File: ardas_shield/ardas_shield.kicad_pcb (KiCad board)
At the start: 2 copper layers, 68.8 x 53.4 mm, 39 parts, among them CON1 SD_Card, IC1 DS1307, P1 CONN_10, P10 CONN_01X03, P2 CONN_8, P3 CONN_8, P4 CONN_ICSP, P5 CONN_6, P6 TTL_COMM, P7 CONN_01X03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

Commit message: rename Ardas
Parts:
- V4, V5, V6: footprint 1pin -> kicad-gfa local:MountingHole_3mm
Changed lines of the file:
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@@
     (links 152)
     (no_connects 0)
-    (area 26.206268 60.1726 264.729686 136.733281)
+    (area 46.862999 67.932299 116.078001 121.716801)
     (thickness 1.6002)
     (drawings 68)
@@
     )
   )
-  (module 1pin locked (layer Front)
-    (at 113.005 113.876)
-    (descr "module 1 pin (ou trou mecanique de percage)")
-    (tags DEV)
-    (path 1pin)
-    (fp_text reference V5 (at 0 -3.048) (layer F.SilkS) hide
-      (effects (font (size 1.016 1.016) (thickness 0.254)))
-    )
-    (fp_text value "" (at 0 2.794) (layer F.SilkS) hide
-      (effects (font (size 1.016 1.016) (thickness 0.254)))
-    )
-    (fp_circle (center 0.00254 0.00254) (end 1.39192 1.04648) (layer F.SilkS) (width 0.381))
-    (pad 1 thru_hole circle (at 0 0) (size 2.54 2.54) (drill 2.54) (layers *.Cu *.Mask F.SilkS))
-  )
   (module Pin_Headers:Pin_Header_Straight_1x08 locked (layer Back)
     (at 74.93 119.037 270)
@@
       (rotate (xyz 0 0 90))
     )
-  )
-  (module 1pin locked (layer Front)
-    (at 113.081 85.885)
-    (descr "module 1 pin (ou trou mecanique de percage)")
-    (tags DEV)
-    (path 1pin)
-    (fp_text reference V4 (at -2.29108 1.61036) (layer F.SilkS) hide
-      (effects (font (size 1.016 1.016) (thickness 0.254)))
-    )
-    (fp_text value "" (at 0 2.794) (layer F.SilkS) hide
-      (effects (font (size 1.016 1.016) (thickness 0.254)))
-    )
-    (fp_circle (center 0.00254 0.00254) (end 1.53924 0.81026) (layer F.SilkS) (width 0.381))
-    (pad 1 thru_hole circle (at 0 0) (size 2.54 2.54) (drill 2.54) (layers *.Cu *.Mask F.SilkS))
-  )
-  (module 1pin locked (layer Front)
-    (at 62.2808 70.8736)
-    (descr "module 1 pin (ou trou mecanique de percage)")
-    (tags DEV)
-    (path 1pin)
-    (fp_text reference V6 (at 4.6736 -8.6614) (layer F.SilkS) hide
-      (effects (font (size 1.016 1.016) (thickness 0.254)))
-    )
-    (fp_text value "" (at 0 2.794) (layer F.SilkS) hide
-      (effects (font (size 1.016 1.016) (thickness 0.254)))
-    )
-    (fp_circle (center 0 0.00508) (end 1.45288 0.93472) (layer F.SilkS) (width 0.381))
-    (pad 1 thru_hole circle (at 0 0) (size 2.54 2.54) (drill 2.54) (layers *.Cu *.Mask F.SilkS))
   )
   (module Capacitors_SMD:C_0805 (layer Front)
@@
     (tags "resistor array")
     (attr smd)
-    (fp_text reference RP1 (at 0 -3.5 180) (layer F.SilkS)
+    (fp_text reference RP1 (at 0 -3.556 180) (layer F.SilkS)
       (effects (font (size 1 1) (thickness 0.15)))
     )
@@
   (module RTC_Ardas_test:small_no_jumper (layer Front)
     (at 48.768 74.1553 270)
-    (fp_text reference JP1 (at 0 2.54 270) (layer F.SilkS)
+    (fp_text reference JP1 (at 0 -2.54 270) (layer F.SilkS)
       (effects (font (size 1 1) (thickness 0.15)))
     )
@@
       (net 1 GND) (solder_mask_margin 0.5))
   )
+  (module "kicad-gfa local:MountingHole_3mm" locked (layer Front)
+    (at 62.2808 70.8736)
+    (descr "Mounting hole, Befestigungsbohrung, 3mm, No Annular, Kein Restring,")
+    (tags "Mounting hole, Befestigungsbohrung, 3mm, No Annular, Kein Restring,")
+    (path 1pin)
+    (fp_text reference V6 (at 0 -4.0005) (layer F.SilkS) hide
+      (effects (font (size 1 1) (thickness 0.15)))
+    )
+    (fp_text value "" (at 1.00076 5.00126) (layer F.Fab) hide
+      (effects (font (size 1 1) (thickness 0.15)))
+    )
+    (fp_circle (center 0 0) (end 3 0) (layer Cmts.User) (width 0.381))
+    (pad 1 thru_hole circle (at 0 0) (size 3 3) (drill 3) (layers))
+  )
+  (module "kicad-gfa local:MountingHole_3mm" locked (layer Front)
+    (at 113.081 85.885)
+    (descr "Mounting hole, Befestigungsbohrung, 3mm, No Annular, Kein Restring,")
+    (tags "Mounting hole, Befestigungsbohrung, 3mm, No Annular, Kein Restring,")
+    (path 1pin)
+    (fp_text reference V4 (at 0 -4.0005) (layer F.SilkS) hide
+      (effects (font (size 1 1) (thickness 0.15)))
+    )
+    (fp_text value "" (at 1.00076 5.00126) (layer F.Fab) hide
+      (effects (font (size 1 1) (thickness 0.15)))
+    )
+    (fp_circle (center 0 0) (end 3 0) (layer Cmts.User) (width 0.381))
+    (pad 1 thru_hole circle (at 0 0) (size 3 3) (drill 3) (layers))
+  )
+  (module "kicad-gfa local:MountingHole_3mm" locked (layer Front)
+    (at 113.005 113.876)
+    (descr "Mounting hole, Befestigungsbohrung, 3mm, No Annular, Kein Restring,")
+    (tags "Mounting hole, Befestigungsbohrung, 3mm, No Annular, Kein Restring,")
+    (path 1pin)
+    (fp_text reference V5 (at 0 -4.0005) (layer F.SilkS) hide
+      (effects (font (size 1 1) (thickness 0.15)))
+    )
+    (fp_text value "" (at 1.00076 5.00126) (layer F.Fab) hide
+      (effects (font (size 1 1) (thickness 0.15)))
+    )
+    (fp_circle (center 0 0) (end 3 0) (layer Cmts.User) (width 0.381))
+    (pad 1 thru_hole circle (at 0 0) (size 3 3) (drill 3) (layers))
+  )
   (gr_text "ArDAS shield\n01-2016" (at 101.727 75.1078) (layer F.SilkS)

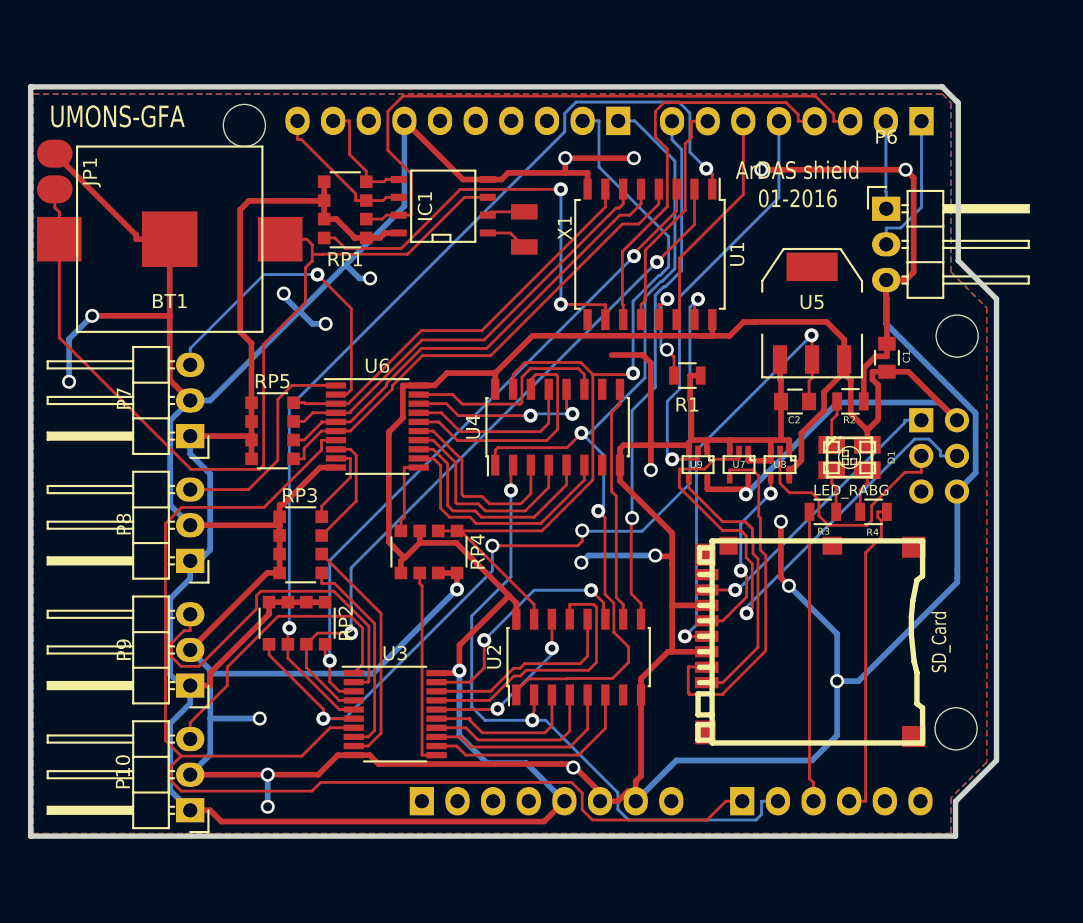
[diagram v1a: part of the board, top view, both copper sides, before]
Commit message: Updated ardas_shield geometry and microSD. Rerouted shield
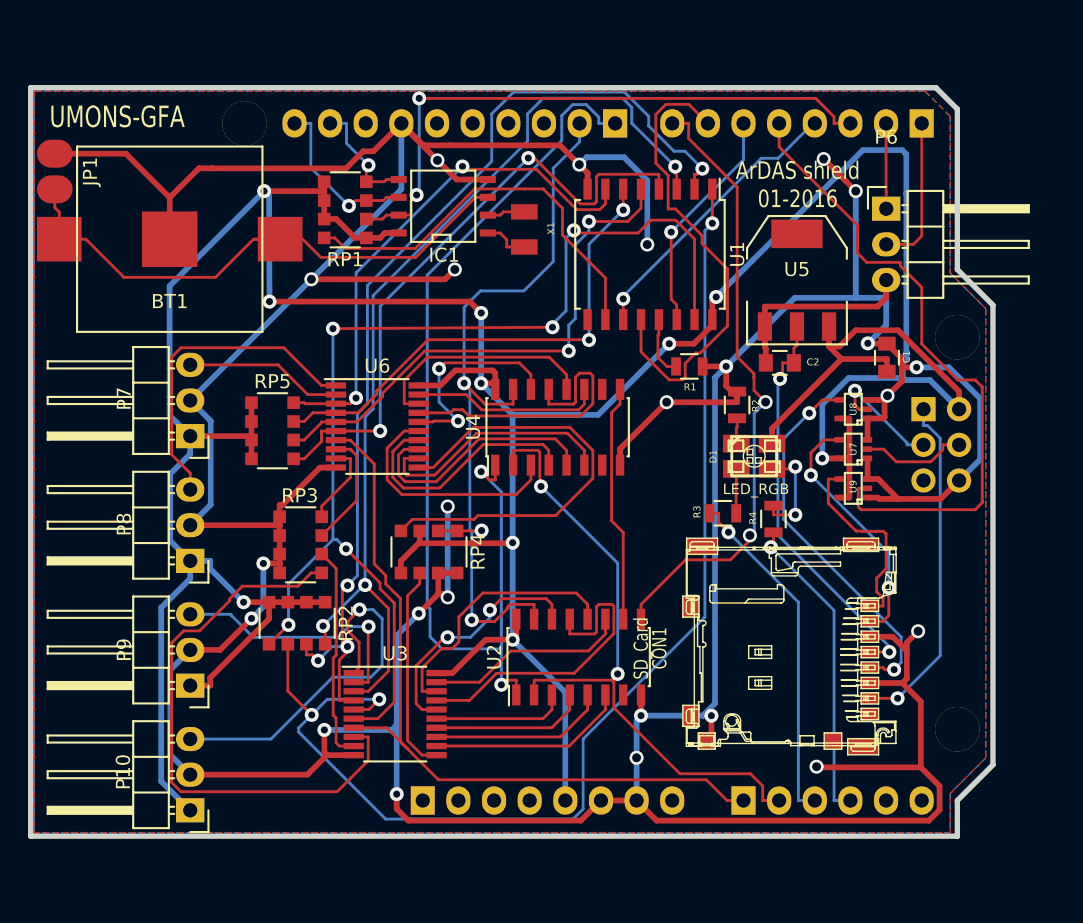
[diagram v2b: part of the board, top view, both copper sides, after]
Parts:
- CON1: footprint MyFootprints:microsd_socket -> kicad-gfa local:microSD_socket
- D1: value LED_RABG -> LED_RGB
- V4, V5, V6: footprint kicad-gfa local:MountingHole_3mm -> kicad-gfa local:MountingHole_125mil
- moved U9 11.2 mm to (105.7, 96.7), turned to 90 degrees
- moved U7 8.22 mm to (105.7, 93.9), turned to 90 degrees
- moved R2 8.08 mm to (97.4, 90.8), turned to 90 degrees
- moved R4 7.15 mm to (100.0, 98.9), turned to 270 degrees
- moved R3 7.13 mm to (96.4, 98.5)
- moved D1 6.80 mm to (98.6, 94.4)
- moved U8 6.55 mm to (105.7, 91.1), turned to 90 degrees
- moved C2 2.96 mm to (100.4, 87.8)
- moved U5 2.59 mm to (101.7, 81.9)
- moved CON1 1.51 mm to (101.3, 108.5), turned to 270 degrees
- moved P4 0.80 mm to (110.7, 91.1)
- moved R1 0.66 mm to (94.0, 88.0)
- moved P1 0.28 mm to (88.7, 70.7)
- moved P3 0.15 mm to (110.6, 70.7)
- moved V6 0.15 mm to (62.3, 70.7)
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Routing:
- net D14: track 90.9 -> 54.6 mm
- net +5V: track 249.4 -> 284.2 mm, vias 2 -> 10
- net MOSI: track 41.2 -> 7.62 mm, vias 1 -> 0
- net Net-(RP4-Pad4): track 5.64 -> 31.5 mm
- net Net-(RP3-Pad1): track 15.0 -> 40.7 mm
- net Net-(BT1-Pad1): track 63.1 -> 40.7 mm
- net Net-(RP2-Pad5): track 58.6 -> 79.9 mm, vias 4 -> 5
- net GND: track 377.5 -> 398.3 mm, vias 20 -> 24
- net Net-(RP2-Pad7): track 51.3 -> 72.0 mm, vias 2 -> 4
- net Net-(RP2-Pad8): track 48.6 -> 69.2 mm, vias 2 -> 3
- net Net-(RP2-Pad6): track 68.9 -> 85.9 mm, vias 2 -> 3
- net D06: track 16.8 -> 33.5 mm
- net D04: track 30.0 -> 46.3 mm, vias 1 -> 0
- net /SCK3: track 13.0 -> 27.0 mm
- net CH4: track 22.9 -> 11.3 mm, vias 1 -> 0
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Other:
- board size 68.8 x 53.4 mm -> 68.6 x 53.3 mm

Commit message: updated to v0.49
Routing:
- net Net-(D1-Pad3): track 7.38 -> 2.66 mm, vias 2 -> 0
- net GND: track 398.3 -> 396.4 mm, vias 24 -> 23
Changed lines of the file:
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@@
 (kicad_pcb (version 4) (host pcbnew 4.0.1-3.201512221402+6198~38~ubuntu14.04.1-stable)
   (general
-    (links 153)
+    (links 152)
     (no_connects 0)
-    (area 46.862999 67.995799 115.824001 121.716801)
+    (area 46.862999 60.1726 264.729686 132.9182)
     (thickness 1.6002)
     (drawings 63)
-    (tracks 1034)
+    (tracks 1028)
     (zones 0)
     (modules 39)
@@
     (title ArDAS_shield)
     (date 2016-01-13)
-    (rev 0.48)
+    (rev 0.49)
     (company UMONS-GFA)
     (comment 1 O.KAUFMANN)
@@
     (mod_text_width 0.3048)
     (pad_size 1.16 1.2)
-    (pad_drill 0.6)
+    (pad_drill 0)
     (pad_to_mask_clearance 0.254)
     (aux_axis_origin 125.349 130.2258)
@@
     (pad 1 smd rect (at -3.38328 -5.52196 270) (size 0.8 1.25) (layers Front F.Paste F.Mask)
       (net 5 /SEN3) (solder_mask_margin 0.1016) (clearance 0.254))
-    (pad GND smd rect (at 6.21792 6.11124 270) (size 1.16 1.2) (layers Front F.Paste F.Mask)
-      (net 1 GND) (solder_mask_margin 0.1016) (clearance 0.254))
+    (pad CD1 smd rect (at 6.21792 6.11124 270) (size 1.16 1.2) (layers Front F.Paste F.Mask)
+      (solder_mask_margin 0.1016) (clearance 0.254))
     (pad 9 smd rect (at 4.43992 7.25424 270) (size 1.5 1.15) (layers Front F.Paste F.Mask)
       (solder_mask_margin 0.1016) (clearance 0.254))
@@
     (effects (font (size 0.762 0.635) (thickness 0.16002)) (justify mirror))
   )
+  (segment (start 65.659 84.2518) (end 65.659 83.2358) (width 0.4064) (layer Back) (net 1))
+  (segment (start 65.659 83.2358) (end 65.8495 83.0453) (width 0.4064) (layer Back) (net 1))
+  (segment (start 67.056 81.8388) (end 65.8495 83.0453) (width 0.4064) (layer Back) (net 1))
+  (segment (start 58.42 90.4748) (end 63.9445 84.9503) (width 0.4064) (layer Back) (net 1))
+  (segment (start 63.9445 84.9503) (end 64.9605 84.9503) (width 0.4064) (layer Back) (net 1))
+  (segment (start 64.9605 84.9503) (end 65.659 84.2518) (width 0.4064) (layer Back) (net 1))
   (via (at 108.117049 90.133834) (size 1) (drill 0.635) (layers Front Back) (net 1))
   (segment (start 108.1405 90.1573) (end 108.1405 90.157285) (width 0.4064) (layer Back) (net 1))
@@
   (via (at 90.2335 115.9383) (size 1) (drill 0.635) (layers Front Back) (net 1))
   (segment (start 67.056 81.8388) (end 76.581 81.8388) (width 0.4064) (layer Front) (net 1))
-  (via (at 77.2795 81.1403) (size 1) (drill 0.635) (layers Front Back) (net 1))
   (segment (start 76.581 81.8388) (end 77.2795 81.1403) (width 0.4064) (layer Front) (net 1))
+  (via (at 77.2795 81.1403) (size 1) (drill 0.635) (layers Front Back) (net 1))
   (via (at 76.0409 73.3619) (size 1) (drill 0.635) (layers Front Back) (net 1))
   (segment (start 76.0409 73.3619) (end 76.0095 73.3933) (width 0.4064) (layer Back) (net 1))
@@
   (segment (start 106.693 96.0755) (end 107.4547 96.0755) (width 0.4064) (layer Front) (net 1))
   (segment (start 107.4547 96.0755) (end 108.8745 97.4953) (width 0.4064) (layer Front) (net 1))
-  (segment (start 95.5675 112.9411) (end 95.5675 114.39418) (width 0.4064) (layer Front) (net 1))
-  (segment (start 95.5675 114.39418) (end 95.23476 114.72692) (width 0.4064) (layer Front) (net 1))
   (via (at 74.7082 105.658) (size 1) (layers Front Back) (net 1))
   (segment (start 74.7082 105.658) (end 73.1361 107.23) (width 0.4064) (layer Back) (net 1))
@@
   (via (at 106.713 86.4045) (size 1) (layers Front Back) (net 1))
   (via (at 90.551 112.935) (size 1) (layers Front Back) (net 1))
-  (via (at 95.5675 112.9411) (size 1) (layers Front Back) (net 1))
   (via (at 63.6349 102.092) (size 1) (layers Front Back) (net 1))
   (via (at 110.19 88.1122) (size 1) (layers Front Back) (net 1))
@@
   (segment (start 76.8892 72.2887) (end 75.0319 72.2887) (width 0.4064) (layer Front) (net 1))
   (segment (start 73.4695 75.4253) (end 67.056 81.8388) (width 0.4064) (layer Back) (net 1))
-  (segment (start 67.056 81.8388) (end 58.42 90.4748) (width 0.4064) (layer Back) (net 1))
   (segment (start 73.4695 70.7263) (end 73.4695 75.4253) (width 0.4064) (layer Back) (net 1))
   (segment (start 99.378 86.6974) (end 99.378 85.2043) (width 0.4064) (layer Front) (net 1))
@@
   (segment (start 64.794 102.092) (end 64.794 101.422) (width 0.4064) (layer Front) (net 1))
   (segment (start 90.551 112.935) (end 94.9549 112.935) (width 0.4064) (layer Back) (net 1))
-  (segment (start 94.9549 112.935) (end 95.5675 112.9411) (width 0.4064) (layer Back) (net 1))
-  (segment (start 95.2348 114.727) (end 95.2348 114.7269) (width 0.4064) (layer Front) (net 1))
   (segment (start 97.3963 89.8423) (end 97.3963 90.2206) (width 0.4064) (layer Front) (net 1))
   (segment (start 64.794 98.762) (end 64.794 99.365) (width 0.4064) (layer Front) (net 1))
@@
   (segment (start 97.3963 92.3974) (end 97.3455 92.4482) (width 0.2032) (layer Front) (net 82))
   (segment (start 97.3963 91.7423) (end 97.3963 92.3974) (width 0.2032) (layer Front) (net 82))
-  (via (at 101.549 98.6254) (size 1) (layers Front Back) (net 83))
-  (via (at 101.549 95.1942) (size 1) (layers Front Back) (net 83))
-  (segment (start 99.9871 98.6254) (end 101.549 98.6254) (width 0.2032) (layer Front) (net 83))
-  (segment (start 99.9871 97.9703) (end 99.9871 98.6254) (width 0.2032) (layer Front) (net 83))
-  (segment (start 101.549 95.1942) (end 101.549 98.6254) (width 0.2032) (layer Back) (net 83))
-  (segment (start 101.296 95.1942) (end 101.549 95.1942) (width 0.2032) (layer Front) (net 83))
-  (segment (start 101.141 95.3499) (end 101.296 95.1942) (width 0.2032) (layer Front) (net 83))
-  (segment (start 99.8855 95.3499) (end 101.141 95.3499) (width 0.2032) (layer Front) (net 83))
+  (segment (start 99.9871 97.9703) (end 99.9871 95.4515) (width 0.2032) (layer Front) (net 83))
+  (segment (start 99.9871 95.4515) (end 99.8855 95.3499) (width 0.2032) (layer Front) (net 83))
   (segment (start 97.3303 96.3052) (end 97.3303 98.5139) (width 0.2032) (layer Front) (net 84))
   (segment (start 97.3455 96.29) (end 97.3303 96.3052) (width 0.2032) (layer Front) (net 84))

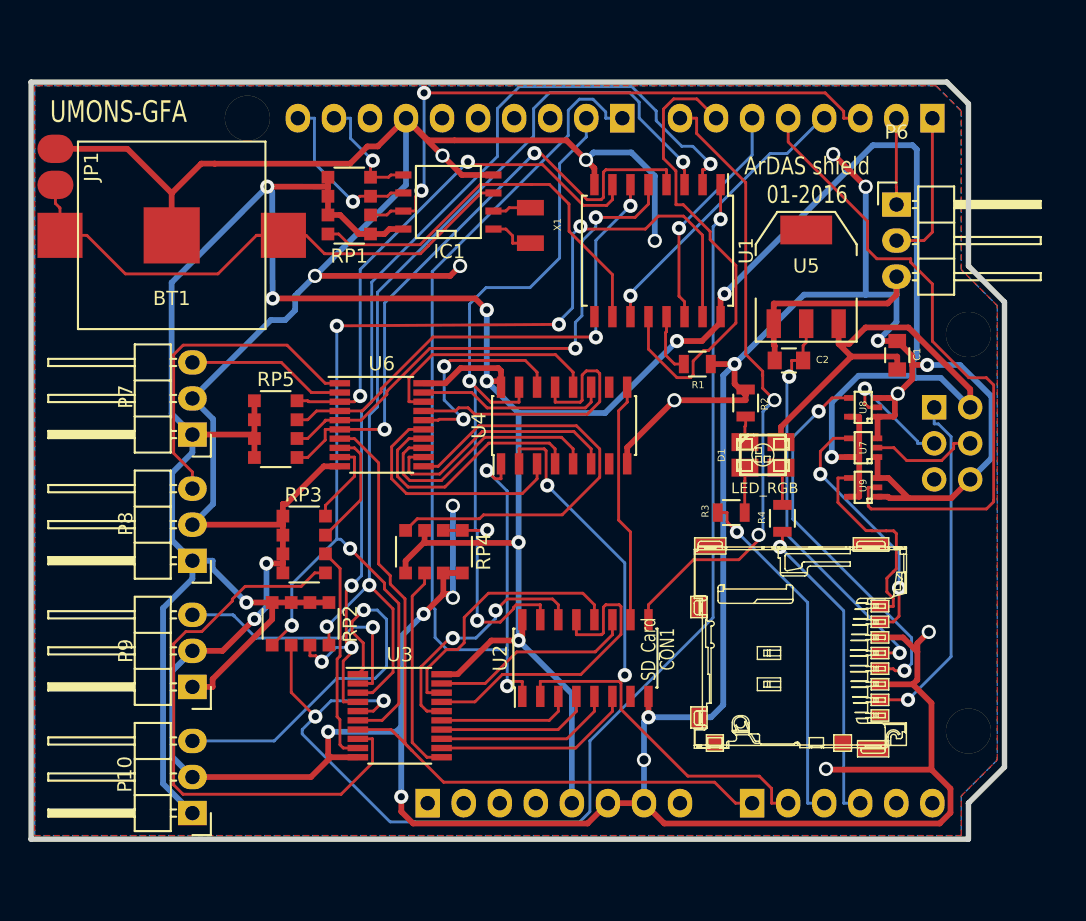
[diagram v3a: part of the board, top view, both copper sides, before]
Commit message: changed resitances arrays footprints
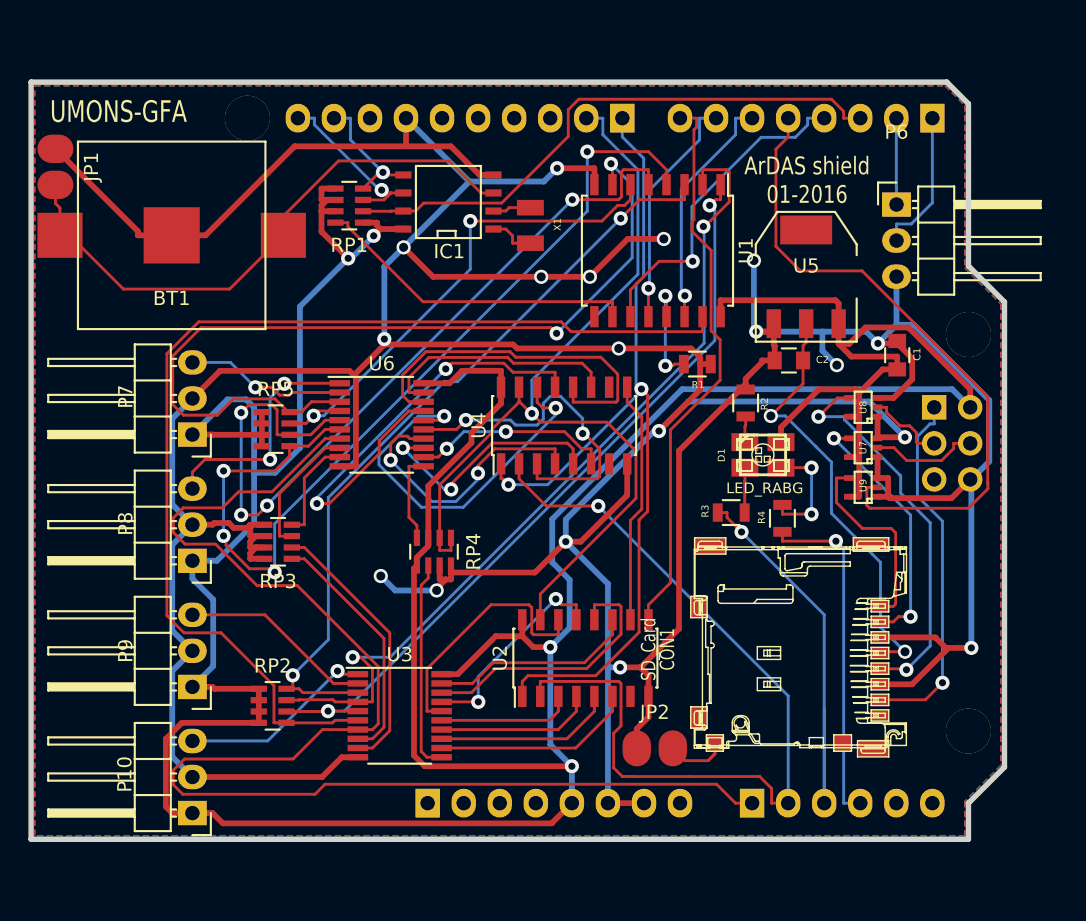
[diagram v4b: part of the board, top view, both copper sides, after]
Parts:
- added JP2: Jumper_NO_Small, RTC_Ardas_test:small_no_jumper, F.Cu at (91.0, 115.1)
- D1: value LED_RGB -> LED_RABG
- RP1, RP2, RP3, RP4, RP5: footprint Resistors_SMD:R_Array_Convex_4x1206 -> kicad-gfa local:R_Array_Convex_4x0603
- moved RP2 6.10 mm to (64.1, 112.1), turned to 0 degrees
- moved RP3 1.85 mm to (64.5, 100.6)
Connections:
- net D18 renamed Net-(P5-Pad5)
- net D19 renamed Net-(P5-Pad6)
- CON1 pad CD1: (no net) -> Net-(CON1-PadCD1)
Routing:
- net D14: track 54.6 -> 96.2 mm
- net Net-(RP2-Pad6): track 85.9 -> 54.8 mm, vias 3 -> 2
- net Net-(RP4-Pad4): track 31.5 -> 6.30 mm
- net Net-(RP5-Pad8): track 37.0 -> 61.0 mm
- net Net-(RP3-Pad1): track 40.7 -> 17.3 mm
- net Net-(RP5-Pad5): track 44.9 -> 65.3 mm, vias 2 -> 4
- net Net-(RP5-Pad6): track 37.7 -> 57.6 mm, vias 2 -> 4
- net D06: track 33.5 -> 16.6 mm, vias 0 -> 1
- net D15: track 45.5 -> 60.8 mm, vias 2 -> 1
- net Net-(RP2-Pad8): track 69.2 -> 54.5 mm, vias 3 -> 2
- net CH1: track 26.4 -> 13.8 mm
- net Net-(U4-Pad14): track 15.2 -> 27.4 mm
- net Net-(RP2-Pad7): track 72.0 -> 60.0 mm, vias 4 -> 2
- net Net-(U4-Pad13): track 21.3 -> 33.2 mm, vias 0 -> 2
- net D09: track 56.0 -> 66.0 mm, vias 3 -> 1
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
